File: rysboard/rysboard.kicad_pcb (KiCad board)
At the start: 2 copper layers, 56 x 65 mm, 85 parts, among them J1 RPi4, J10 ToF3, J11 ToF4, J12 ToF5, J13 ToF6, J14 SPI, J15 Temp, J16 IMU, J17 Conn_01x03, J2 Motor L, J3 Motor R, J4 CELL3, J5 CELL2, J6 CELL1, J7 SW, J8 ToF1, J9 ToF2, Q1 MBT3946DW1T1, U1 L6470, U2 L6470, U3 ST1S10PHR, U4 MAX11613, U5 74AHC2G00

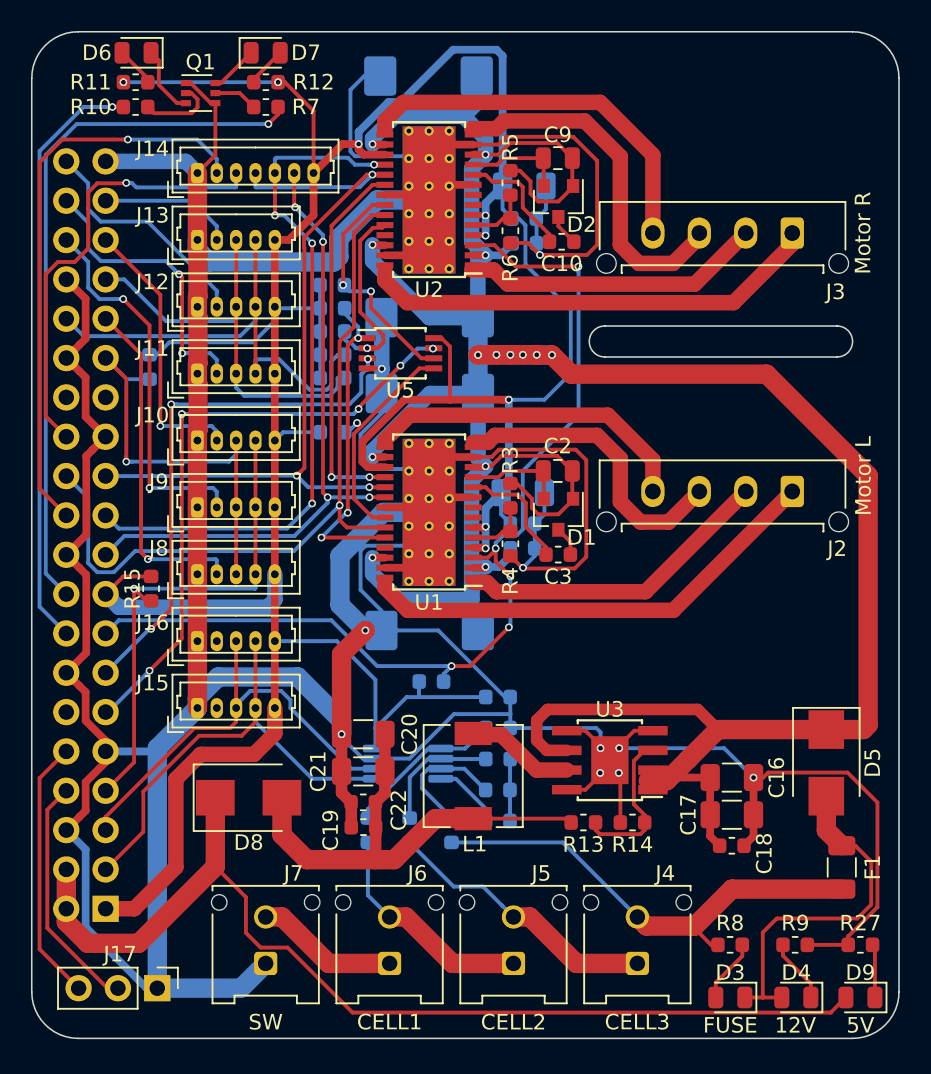
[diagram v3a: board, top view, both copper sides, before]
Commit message: rysboard v4.2: * re-add mountting holes * fix some layout errors * add ground fills * ensure proper track width * add front-side filkscreen
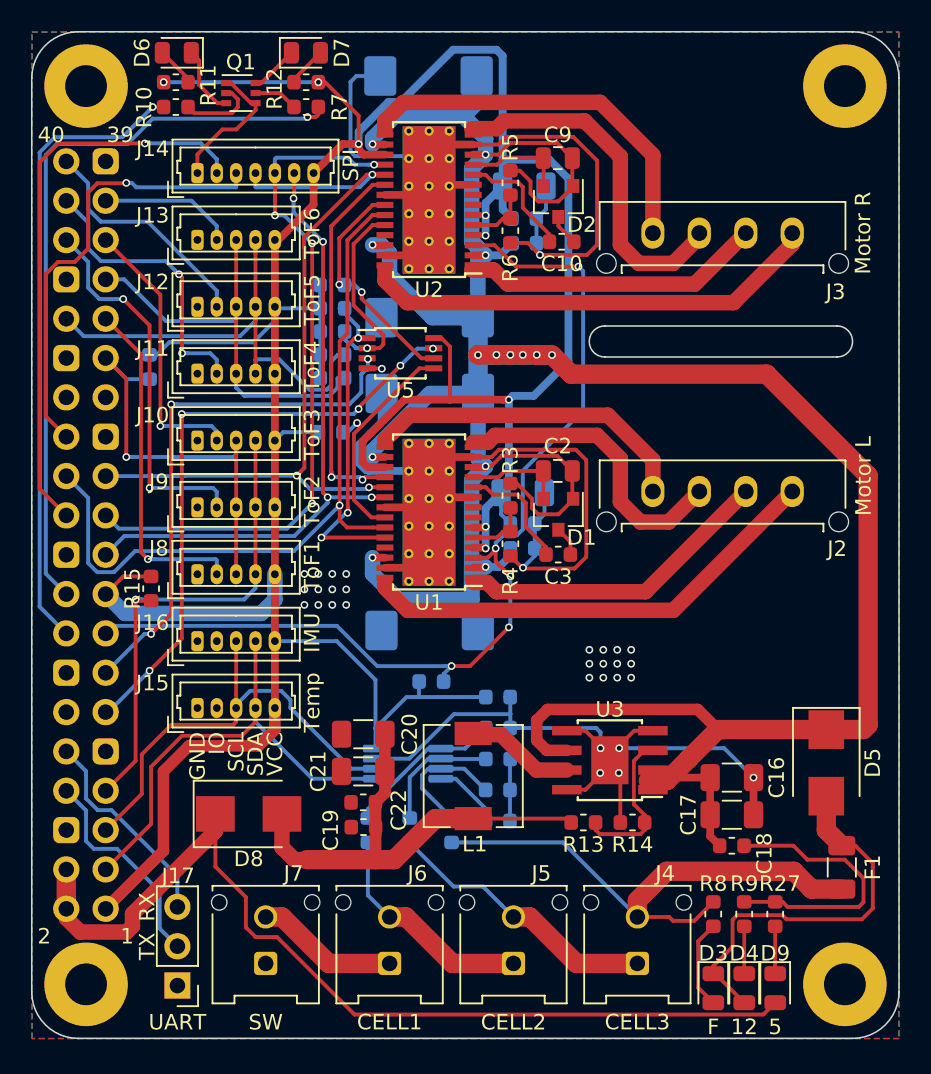
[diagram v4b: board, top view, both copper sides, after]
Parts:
- added H1: MountingHole_Pad, MountingHole:MountingHole_2.7mm_M2.5_Pad, F.Cu at (78.8, 127.2)
- added H2: MountingHole_Pad, MountingHole:MountingHole_2.7mm_M2.5_Pad, F.Cu at (78.8, 69.2)
- added H3: MountingHole_Pad, MountingHole:MountingHole_2.7mm_M2.5_Pad, F.Cu at (127.8, 69.2)
- added H4: MountingHole_Pad, MountingHole:MountingHole_2.7mm_M2.5_Pad, F.Cu at (127.8, 127.2)
- moved R27 5.85 mm to (123.3, 122.6), turned to 90 degrees
- moved D9 5.53 mm to (123.3, 127.4), turned to 270 degrees
- moved R9 3.84 mm to (121.3, 122.6), turned to 90 degrees
- moved D4 3.42 mm to (121.3, 127.4), turned to 270 degrees
- moved R12 2.60 mm to (93.0, 68.9)
- moved R7 2.60 mm to (93.0, 70.5)
- moved D6 2.60 mm to (84.7, 67.0)
- moved D7 2.60 mm to (93.0, 67.0)
- moved Q1 2.60 mm to (88.8, 69.6)
- moved R10 2.60 mm to (84.6, 70.5)
- moved R11 2.60 mm to (84.6, 68.9)
- moved R8 2.27 mm to (119.3, 122.6), turned to 90 degrees
- moved J17 1.31 mm to (84.7, 127.2), turned to 180 degrees
- moved D3 1.25 mm to (119.3, 127.4), turned to 270 degrees
- moved D8 1.05 mm to (89.3, 116.2)
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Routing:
- net GND: track 409.4 -> 191.8 mm, vias 10 -> 32
- net /Power Supply/V_CELL3: track 30.5 -> 35.0 mm
- net +5V: track 66.5 -> 62.4 mm
- net /UART_RXD: track 17.0 -> 13.5 mm
- net /LED2: track 45.5 -> 48.1 mm
- net /LED1: track 38.5 -> 41.0 mm
- net +3V3: track 216.6 -> 219.1 mm
- net Net-(D3-Pad1): track 23.0 -> 25.4 mm
- net /UART_TXD: track 15.5 -> 13.9 mm
- net Net-(D3-Pad2): track 4.11 -> 5.75 mm
- net Net-(D4-Pad1): track 4.15 -> 3.06 mm
- net /I2C1_SCL: track 29.0 -> 30.0 mm
- net /I2C3_SDA: track 32.6 -> 31.8 mm
- net /I2C1_SDA: track 30.5 -> 31.2 mm
- net Net-(C19-Pad1): track 31.3 -> 30.7 mm
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- added copper zone on B.Cu, net GND
- added copper zone on F.Cu, net GND

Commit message: rysboard v4.2: adjust silkscreen text positions, add board name, minor layout improvements
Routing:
- net GND: track 191.8 -> 180.5 mm, vias 32 -> 41
- net +3V3: track 219.1 -> 225.5 mm, vias 8 -> 12
- net /SPI_MISO: track 45.3 -> 44.7 mm
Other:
- rule via_min_drill: 0.2 -> 0.3
- board text added: "Bionik 2020"
- board text added: "RysBoard v4.2"

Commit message: rysboard v4.2: status LED transistor swapped for BC847BS; PCB design fixes after review (!1)
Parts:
- L1: footprint Inductor_SMD:L_6.3x6.3_H3 -> rysboard:L_6.7x6.7_H2.2
- Q1: value MBT3946DW1T1 -> BC847BS
- moved L1 0.10 mm to (103.9, 113.7)
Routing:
- net GND: track 180.5 -> 173.8 mm, vias 41 -> 60
- net Vdrive: track 204.3 -> 210.4 mm, vias 14 -> 22
- net +3V3: track 225.5 -> 223.2 mm, vias 12 -> 13
- net /Motor Drivers/~FLAG_1: track 21.5 -> 19.4 mm
- net /~SPI_CS1: track 29.0 -> 27.0 mm
- net /MOTOR_BUSY: track 34.4 -> 36.3 mm
- net +5V: track 62.4 -> 61.2 mm
- net /MOTOR_FLAG: track 39.5 -> 40.4 mm
- net /Motor Drivers/~FLAG_2: track 13.2 -> 13.9 mm
- net /I2C5_SCL: track 28.0 -> 27.3 mm
- net /Motor Drivers/SPI_BRIDGE: track 24.4 -> 25.1 mm
- net /I2C3_SDA: track 31.8 -> 31.2 mm
- net /I2C3_SCL: track 27.0 -> 26.5 mm
- net /~MOTOR_STBY: track 65.4 -> 65.5 mm, vias 5 -> 3
- net (no net): vias 0 -> 150
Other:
- board text added: "KNR Bionik 2020"
- board text removed: "Bionik 2020"

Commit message: rysboard: remove additional i2c pullups; increase high-voltage track clearance
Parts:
- removed R15, R16, R17, R18: 3K3, Resistor_SMD:R_0603_1608Metric
- moved C12 0.05 mm to (101.0, 84.2)
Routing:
- net GND: track 173.8 -> 146.8 mm, vias 60 -> 241
- net /I2C5_SDA: track 31.5 -> 22.2 mm
- net /I2C5_SCL: track 27.3 -> 18.7 mm
- net +3V3: track 223.2 -> 229.2 mm
- net Net-(R13-Pad1): track 9.36 -> 14.1 mm, vias 0 -> 2
- net /I2C3_SCL: track 26.5 -> 23.1 mm
- net /SPI_CLK: track 49.5 -> 48.0 mm
- net Vdrive: track 210.4 -> 211.5 mm
- net /MOTOR_BUSY: track 36.3 -> 35.3 mm
- net /I2C3_SDA: track 31.2 -> 30.3 mm
- net /Motor Drivers/SPI_BRIDGE: track 25.1 -> 25.7 mm
- net (no net): vias 150 -> 0
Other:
- net class Power input added: clearance 0.25, trace_width 1, via_dia 1, via_drill 0.5
- net class Power output: clearance 0.2 -> 0.25

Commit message: rysboard: changed LED and sensors' VCC to 5V
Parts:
- removed the J8 at (86.0, 100.7)
- added J10: ToF1, Connector_Molex:Molex_PicoBlade_53047-0510_1x05_P1.25mm_Vertical, F.Cu at (86.0, 100.7)
- D6: value LED_GREEN -> GREEN
- D7: value LED_RED -> RED
- R10, R7: value 4K7 -> 10k
- R11: value 43R -> 680R
- R12: value 82R -> 680R
- R27: value 2k7 -> 680R
- moved R2 5.00 mm to (94.7, 86.5)
- renumbered J9 to J11, J10 to J12, J11 to J13, J12 to J15, J13 to J16, J15 to J8, J16 to J9
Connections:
- J11 pad 5: +3V3 -> +5V
- J12 pad 5: +3V3 -> +5V
- J13 pad 5: +3V3 -> +5V
- J14 pad 7: +3V3 -> +5V
- J15 pad 5: +3V3 -> +5V
- J16 pad 5: +3V3 -> +5V
- J8 pad 5: +3V3 -> +5V
- J9 pad 5: +3V3 -> +5V
- R11 pad 2: +3V3 -> +5V
- R12 pad 1: +3V3 -> +5V
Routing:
- net +5V: track 61.2 -> 126.1 mm, vias 0 -> 2
- net +3V3: track 229.2 -> 178.7 mm, vias 13 -> 9
- net /Motor Drivers/~BUSY_2: track 15.3 -> 20.2 mm
- net /~MOTOR_STBY: track 65.5 -> 69.5 mm, vias 3 -> 2
- net /Motor Drivers/~BUSY_1: track 15.6 -> 19.3 mm
- net GND: track 146.8 -> 149.9 mm, vias 241 -> 310
- net /I2C1_SDA: track 31.2 -> 28.9 mm
- net /UART_TXD: track 13.9 -> 15.4 mm
- net /I2C1_SCL: track 30.0 -> 28.5 mm
- net /MOTOR_FLAG: track 40.6 -> 39.8 mm, vias 5 -> 3
- net Vdrive: track 211.5 -> 210.8 mm, vias 22 -> 20
- net /Motor Drivers/~FLAG_1: track 19.4 -> 20.0 mm
